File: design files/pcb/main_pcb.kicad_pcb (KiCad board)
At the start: 2 copper layers, 19.7 x 99.1 mm, 42 parts, among them J7 HDR-M-2.54_1x9, U1 ARDUINO_NANO, U2 TL072CP, U3 7805

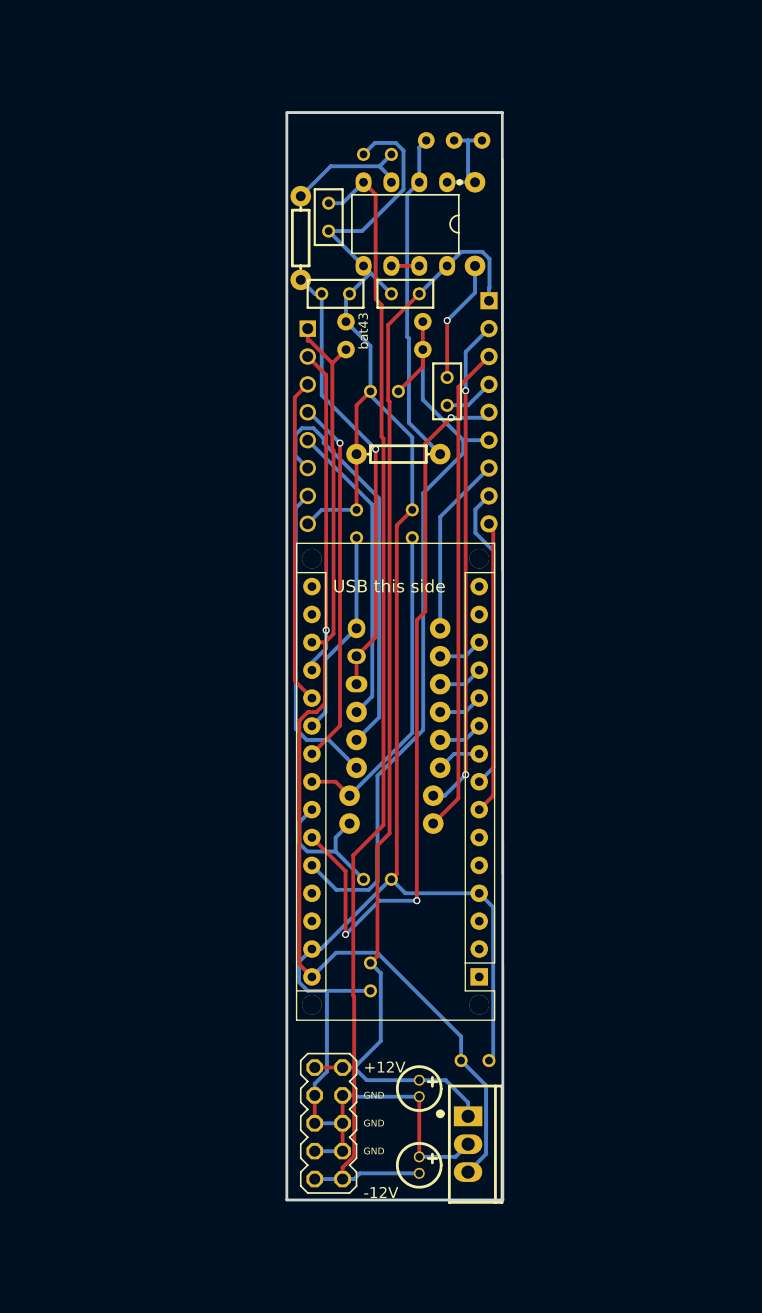
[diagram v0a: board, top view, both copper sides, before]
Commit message: revision 1.1 pcb
mainly better footprints, slightly more space for the power adapter
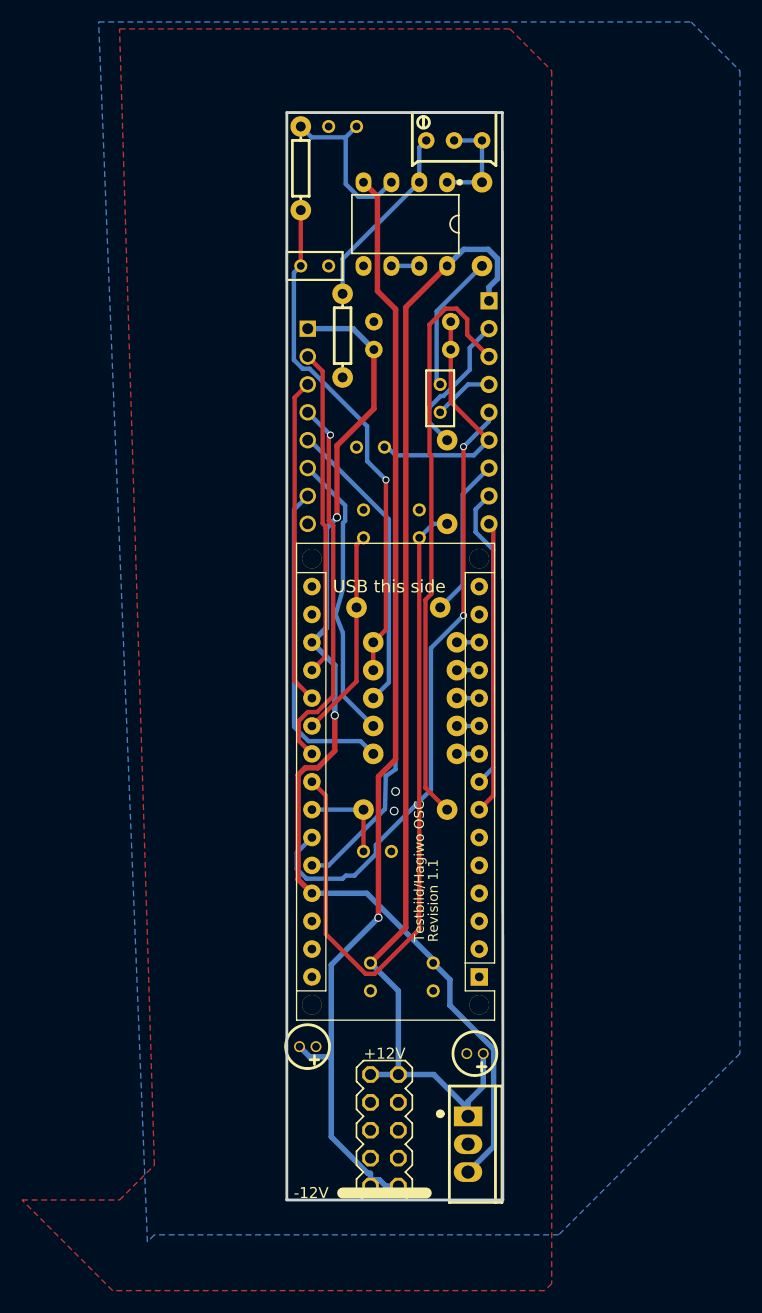
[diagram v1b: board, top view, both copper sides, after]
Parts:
- removed the ? at (-22.2, 200.3)
- removed the ? at (-24.8, 207.9)
- removed the ? at (-24.8, 200.3)
- removed the ? at (-22.2, 210.4)
- removed the ? at (-24.8, 210.4)
- removed the ? at (-22.2, 202.8)
- removed the ? at (-24.8, 202.8)
- removed the ? at (-22.2, 205.4)
- removed the ? at (-24.8, 205.4)
- removed the ? at (-22.2, 207.9)
- removed C12: 4.7n, easyeda:RAD-0.1
- removed C13: 100n, easyeda:RAD-0.1
- removed J7: HDR-M-2.54_1x9, easyeda:HDR-M-2.54_1X9
- added ?: , AutoGenerated:Pad_1.41mm, F.Cu at (-17.1, 200.9)
- added ?: , AutoGenerated:Pad_1.41mm, F.Cu at (-19.7, 208.5)
- added ?: , AutoGenerated:Pad_1.41mm, F.Cu at (-19.7, 200.9)
- added ?: , AutoGenerated:Pad_1.41mm, F.Cu at (-17.1, 211.1)
- added ?: , AutoGenerated:Pad_1.41mm, F.Cu at (-19.7, 211.1)
- added ?: , AutoGenerated:Pad_1.41mm, F.Cu at (-17.1, 203.5)
- added ?: , AutoGenerated:Pad_1.41mm, F.Cu at (-19.7, 203.5)
- added ?: , AutoGenerated:Pad_1.41mm, F.Cu at (-17.1, 206.0)
- added ?: , AutoGenerated:Pad_1.41mm, F.Cu at (-19.7, 206.0)
- added ?: , AutoGenerated:Pad_1.41mm, F.Cu at (-17.1, 208.5)
- added J1: HDR-M-2.54_1x9, easyeda:HDR-M-2.54_1X9, F.Cu at (-8.89, 140.6)
- C10, C11: value 4.7n -> 100n
- C2: value 10n -> 4.7n
- C3: value 4.7u -> 4.7n
- C4: value 10u -> 4.7n; footprint easyeda:CAP-D4.0×F1.5 -> easyeda:RAD-0.1
- C5: value 100n -> 10n
- C6: value 10u -> 4.7u; footprint easyeda:CAP-D4.0×F1.5 -> easyeda:RAD-0.1
- C7: value 100n -> 10u; footprint easyeda:RAD-0.1 -> easyeda:CAP-D4.0×F1.5
- C8: value 0.1u -> 10u; footprint easyeda:RAD-0.1 -> easyeda:CAP-D4.0×F1.5
- C9: value 0.22u -> 100n
- R1: value 499k 0.5% -> 22k
- R10: value 22k -> 220
- R11: value 22k -> 47k
- R2: value 3.9k 0.5% -> 22k
- R3: value 4k7 -> 499k 0.5%
- R4: value 4k7 -> 3.9k 0.5%
- R6: value 3.9k 0.5% -> 4k7
- R7: value 220 -> 22k
- R8: value 47k -> 4k7
- R9: value 22k -> 3.9k 0.5%
- moved C4 82.5 mm to (-24.8, 127.3), turned to 0 degrees
- moved C7 69.2 mm to (-25.4, 198.4)
- moved C6 62.9 mm to (-13.3, 139.3)
- moved R9 60.3 mm to (-26.0, 118.4), turned to 90 degrees
- moved C1 50.9 mm to (-19.1, 180.6)
- moved R6 45.7 mm to (-15.6, 169.2), turned to 0 degrees
- moved R11 42.1 mm to (-22.2, 133.6), turned to 90 degrees
- moved R10 37.6 mm to (-9.53, 123.4), turned to -90 degrees
- moved R7 35.6 mm to (-17.1, 158.4), turned to 180 degrees
- moved C2 33.9 mm to (-15.2, 150.7), turned to 90 degrees
- moved R8 27.3 mm to (-15.6, 171.7)
- moved R2 18.9 mm to (-12.7, 146.9), turned to -90 degrees
- moved C3 14.3 mm to (-20.3, 150.7), turned to 90 degrees
- moved R1 14.0 mm to (-16.5, 176.8), turned to 180 degrees
- moved C10 8.91 mm to (-19.7, 192.0), turned to 90 degrees
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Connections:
- C1 pad 1: C1_1 -> GND
- C1 pad 2: GND -> U1_24
- C10 pad 1: GND -> +12V
- C10 pad 2: U1_24 -> GND
- C11 pad 2: U1_21 -> V_OCT
- C2 pad 1: R6_2 -> GND
- C2 pad 2: GND -> U1_23
- C3 pad 1: R7_1 -> GND
- C3 pad 2: OUT -> U1_21
- C4 pad 1: GND -> C4_1
- C4 pad 2: -12V -> GND
- C5 pad 1: GND -> R9_2
- C5 pad 2: -12V -> GND
- C6 pad 1: +12V -> R10_1
- C6 pad 2: GND -> OUT
- C7 pad 1: +12V -> GND
- C7 pad 2: GND -> -12V
- C8 pad 1: GND -> +12V
- C8 pad 2: +5V -> GND
- C9 pad 1: +12V -> GND
- C9 pad 2: GND -> +5V
- R1 pad 1: U1_13 -> U1_24
- R1 pad 2: C1_1 -> P2CV
- R10 pad 1: U1_21 -> R10_1
- R10 pad 2: MODECV -> U2_1
- R11 pad 1: U1_23 -> GND
- R11 pad 2: P1CV -> U2_2
- R2 pad 1: U1_12 -> U1_23
- R2 pad 2: C1_1 -> P1CV
- R3 pad 1: U1_11 -> U1_13
- R3 pad 2: LED1 -> C4_1
- R4 pad 1: U1_10 -> U1_12
- R4 pad 2: LED2 -> C4_1
- R5 pad 1: U1_9 -> U1_11
- R5 pad 2: LED3 -> LED1
- R6 pad 1: C1_1 -> U1_10
- R6 pad 2: R6_2 -> LED2
- R7 pad 1: R7_1 -> U1_21
- R7 pad 2: U2_1 -> MODECV
- R8 pad 1: GND -> U1_9
- R8 pad 2: U2_2 -> LED3
- R9 pad 1: U1_24 -> C4_1
- R9 pad 2: P2CV -> R9_2
- U1 pad 27: (no net) -> +5V
- U1 pad 30: +5V -> (no net)
- U2 pad 3: R6_2 -> R9_2
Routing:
- net GND: track 184.9 -> 0.00 mm, vias 0 -> 2
- net C4_1: track 0.00 -> 46.5 mm, vias 0 -> 1
- net C1_1: track 40.8 -> 0.00 mm, vias 1 -> 0
- net U1_23: track 29.8 -> 64.8 mm
- net P1CV: track 45.3 -> 13.2 mm, vias 2 -> 0
- net R9_2: track 0.00 -> 15.3 mm
- net U2_2: track 30.5 -> 17.1 mm
- net R10_1: track 0.00 -> 12.6 mm
- net R6_2: track 11.7 -> 0.00 mm
- net R7_1: track 11.2 -> 0.00 mm, vias 1 -> 0
- net LED2: track 37.1 -> 26.4 mm
- net GVC: track 66.8 -> 56.5 mm, vias 3 -> 2
- net P2CV: track 44.6 -> 54.0 mm
- net V_OCT: track 70.0 -> 64.1 mm
- net U1_24: track 13.8 -> 8.51 mm
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- added copper zone on B.Cu, net GND
- added copper zone on F.Cu, net GND
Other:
- board text added: "Revision 1.1"
- board text added: "Testbild/Hagiwo OSC"
- board text removed: "GND"
